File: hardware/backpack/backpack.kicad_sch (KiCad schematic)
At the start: 5 parts, among them J2 Conn_02x06_Top_Bottom, J3 Conn_02x06_Top_Bottom, J7 USB_C, J8 MICROMOD-2222, SW1 BTN_PROGRAM

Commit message: start power
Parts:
- added J8: USB_C, cynthion:USB_C_Receptacle_HRO_TYPE-C-31-M-12, symbol Connector:USB_C_Receptacle_USB2.0
- SW1: value BTN_PROGRAM -> ~; lcsc# (none) -> C692468
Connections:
- new net: J8.A1 (GND), J8.A12 (GND), J8.B1 (GND), J8.B12 (GND)
- new net: J8.A4 (VBUS), J8.A9 (VBUS), J8.B4 (VBUS), J8.B9 (VBUS)
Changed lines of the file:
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@@
+	)
+	(symbol
+		(lib_id "Connector:USB_C_Receptacle_USB2.0")
+		(at 201.93 39.37 0)
+		(mirror y)
+		(unit 1)
+		(exclude_from_sim no)
+		(in_bom yes)
+		(on_board yes)
+		(dnp no)
+		(property "Reference" "J8"
+			(at 201.93 16.51 0)
+			(effects
+				(font
+					(size 1.27 1.27)
+				)
+			)
+		)
+		(property "Value" "USB_C"
+			(at 201.93 19.05 0)
+			(effects
+				(font
+					(size 1.27 1.27)
+				)
+			)
+		)
+		(property "Footprint" "cynthion:USB_C_Receptacle_HRO_TYPE-C-31-M-12"
+			(at 198.12 39.37 0)
+			(effects
+				(font
+					(size 1.27 1.27)
+				)
+				(hide yes)
+			)
+		)
+		(property "Datasheet" ""
+			(at 198.12 39.37 0)
+			(effects
+				(font
+					(size 1.27 1.27)
+				)
+				(hide yes)
+			)
+		)
+		(property "Description" "CONN RCPT USB2.0 TYPE-C 16POS"
+			(at 201.93 39.37 0)
+			(effects
+				(font
+					(size 1.27 1.27)
+				)
+				(hide yes)
+			)
+		)
+		(property "Manufacturer" "DEALON"
+			(at 201.93 39.37 0)
+			(effects
+				(font
+					(size 1.27 1.27)
+				)
+				(hide yes)
+			)
+		)
+		(property "Part Number" "USB-TYPE-C-019"
+			(at 201.93 39.37 0)
+			(effects
+				(font
+					(size 1.27 1.27)
+				)
+				(hide yes)
+			)
+		)
+		(property "Substitution" "Yuandi TYPE-611A-T3"
+			(at 201.93 39.37 0)
+			(effects
+				(font
+					(size 1.27 1.27)
+				)
+				(hide yes)
+			)
+		)
+		(pin "A1"
+		)
+		(pin "A12"
+		)
+		(pin "A4"
+		)
+		(pin "A5"
+		)
+		(pin "A6"
+		)
+		(pin "A7"
+		)
+		(pin "A8"
+		)
+		(pin "A9"
+		)
+		(pin "B1"
+		)
+		(pin "B12"
+		)
+		(pin "B4"
+		)
+		(pin "B5"
+		)
+		(pin "B6"
+		)
+		(pin "B7"
+		)
+		(pin "B8"
+		)
+		(pin "B9"
+		)
+		(pin "S1"
+		)
+		(instances
+			(project "backpack"
+				(path "/df6062c3-a570-4505-924c-c7fe32df3670"
+					(reference "J8")
+					(unit 1)
+				)
+			)
+		)
 	)
 	(symbol
@@
 			)
 		)
-		(property "Value" "BTN_PROGRAM"
+		(property "Value" "~"
 			(at 173.99 46.99 0)
 			(effects
@@
 			(at 173.99 50.8 0)
 			(effects
+				(font
+					(size 1.27 1.27)
+				)
+				(hide yes)
+			)
+		)
+		(property "lcsc#" "C692468"
+			(at 173.99 50.8 0)
+			(effects

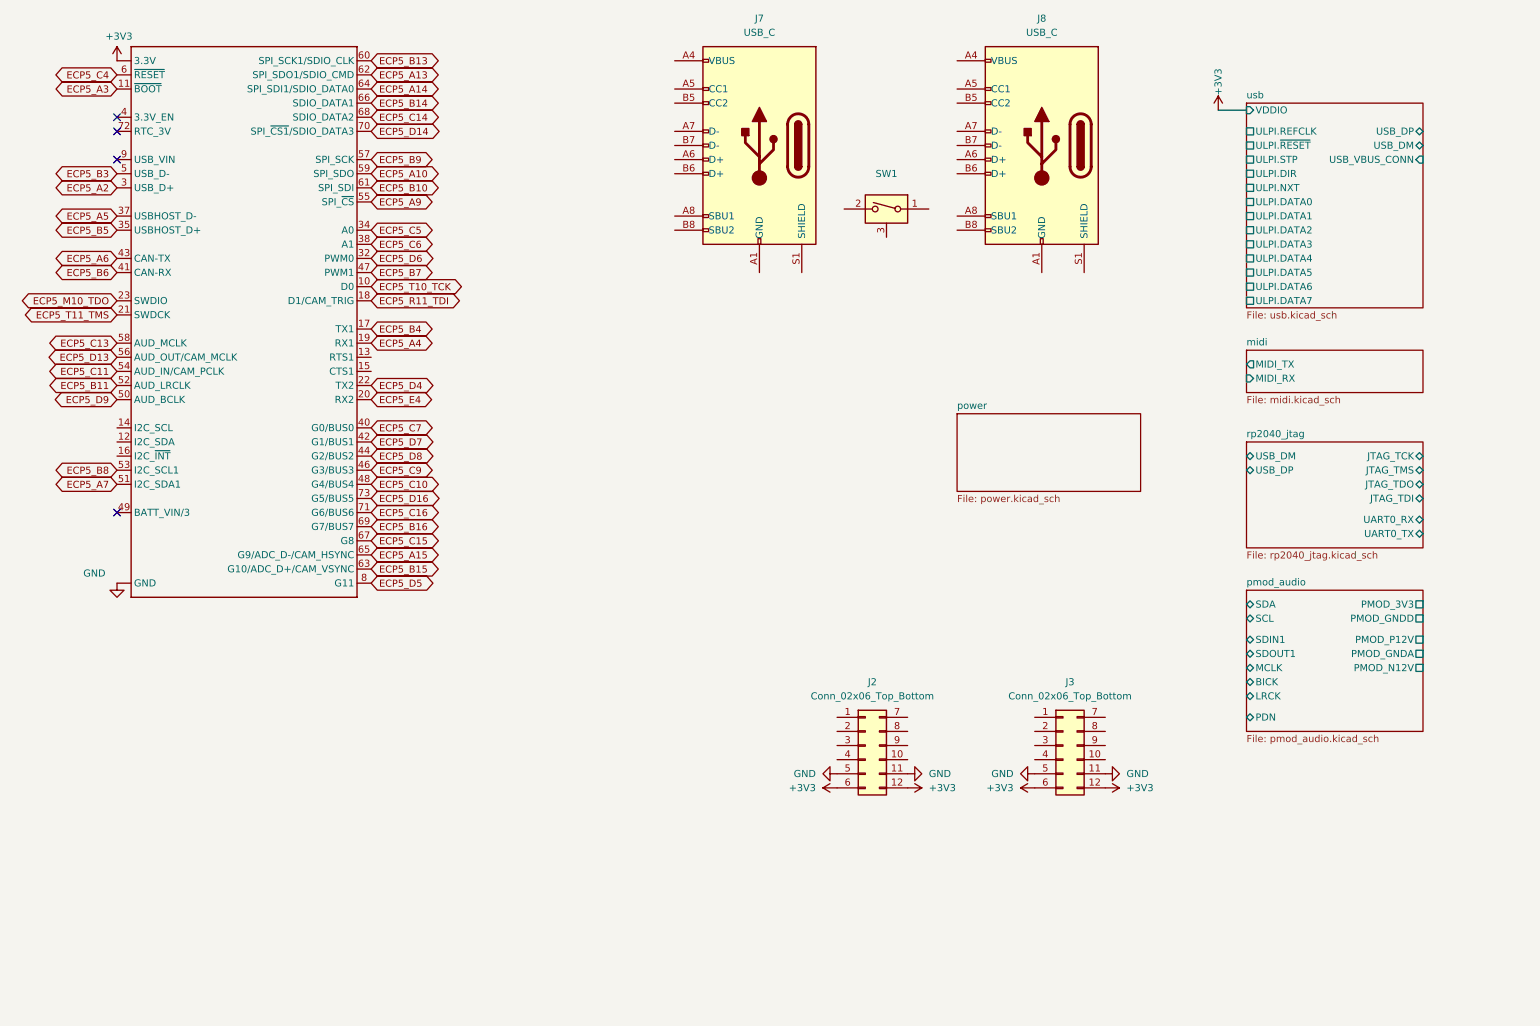
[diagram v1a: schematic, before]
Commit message: parts and capture done sans most needing future pinswaps
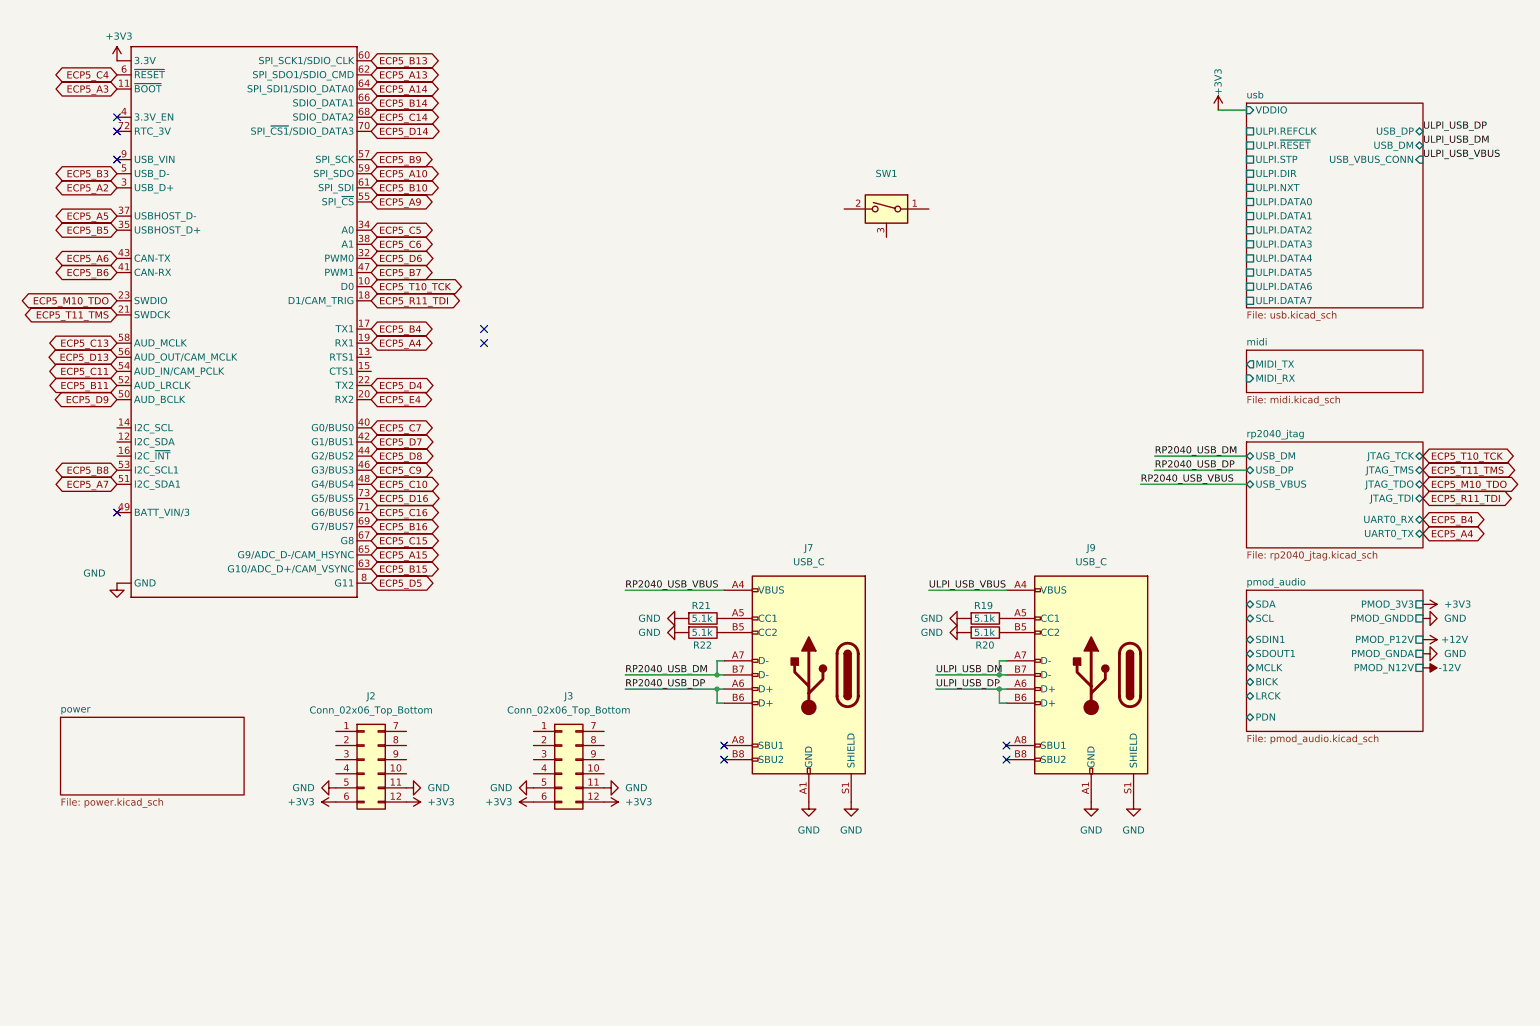
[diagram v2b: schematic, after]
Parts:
- added R19, R20, R21, R22: 5.1k, Resistor_SMD:R_0402_1005Metric, symbol Device:R
- renumbered J8 to J9
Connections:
- net GND: now also J7.A1 (GND), J7.A12 (GND), J7.B1 (GND), J7.B12 (GND), J7.S1 (SHIELD), J9.A1 (GND), J9.A12 (GND), J9.B1 (GND), J9.B12 (GND), J9.S1 (SHIELD), R19.2, R20.2, R21.2, R22.2
- net RP2040_USB_VBUS: now reaches J7.A4 (VBUS), J7.A9 (VBUS), J7.B4 (VBUS), J7.B9 (VBUS)
- net at J7.A5 (CC1): now also R21.1
- net RP2040_USB_DP: now reaches J7.A6 (D+)
- net RP2040_USB_DP: now also J7.B6 (D+)
- net RP2040_USB_DM: now reaches J7.A7 (D-)
- net RP2040_USB_DM: now also J7.B7 (D-)
- net at J7.B5 (CC2): now also R22.1
- net ULPI_USB_VBUS: now reaches J9.A4 (VBUS), J9.A9 (VBUS), J9.B4 (VBUS), J9.B9 (VBUS)
- net at J9.A5 (CC1): now also R19.1
- net ULPI_USB_DP: now reaches J9.A6 (D+)
- net ULPI_USB_DP: now also J9.B6 (D+)
- net ULPI_USB_DM: now reaches J9.A7 (D-)
- net ULPI_USB_DM: now also J9.B7 (D-)
- net at J9.B5 (CC2): now also R20.1
- no-connect marks 4 -> 10
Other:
- sheet rp2040_jtag ports: added USB_VBUS; removed none
- moved on the sheet: J2, J3, J7, J9

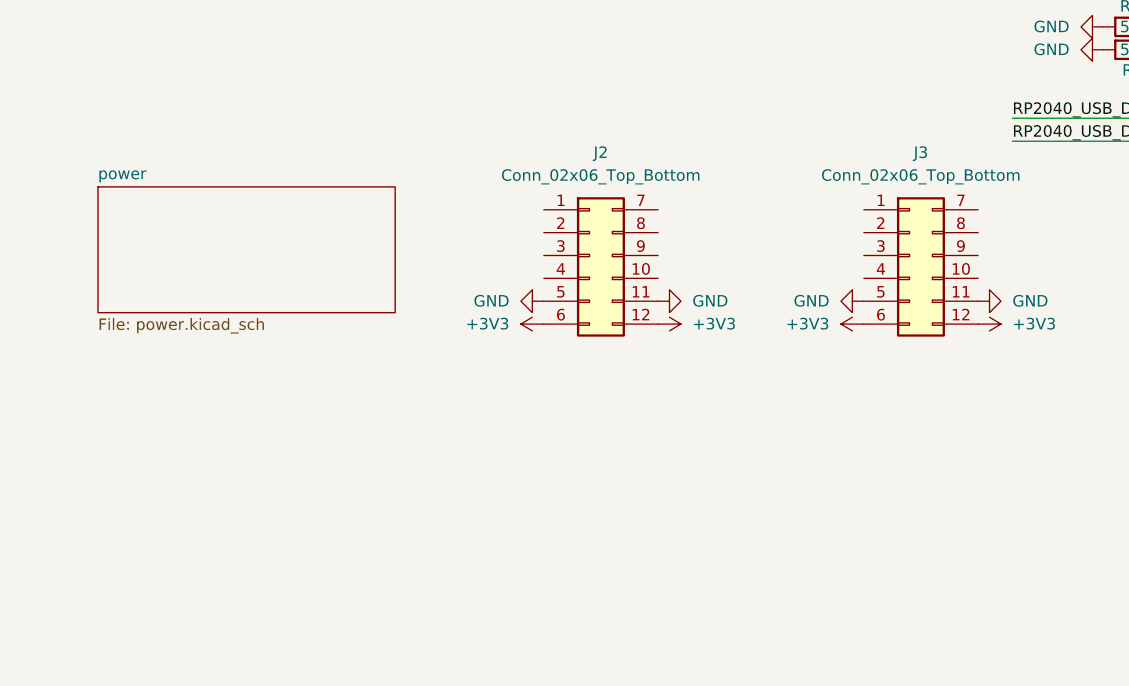
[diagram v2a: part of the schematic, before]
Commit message: aux vin over usb
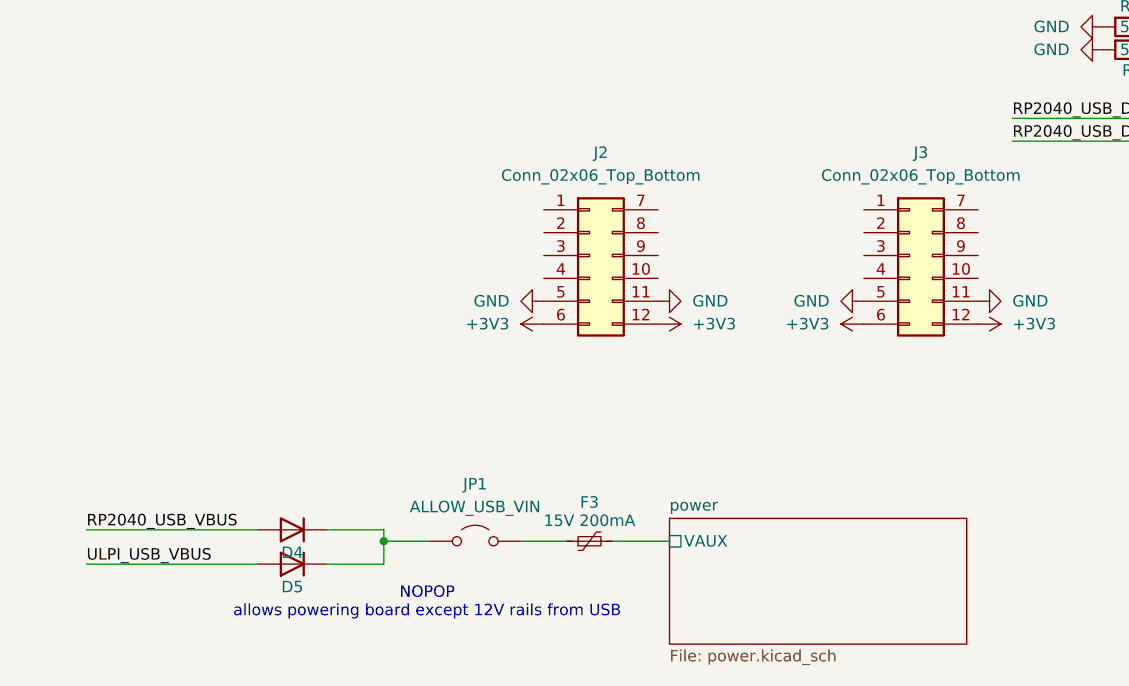
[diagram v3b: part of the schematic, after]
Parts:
- added D4, D5: 1N4007FL, Diode_SMD:D_SOD-123F, symbol Diode:US1G
- added F3: 15V 200mA, Fuse:Fuse_0805_2012Metric, symbol Device:Polyfuse_Small
- added JP1: ALLOW_USB_VIN, symbol Jumper:Jumper_2_Open
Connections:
- net RP2040_USB_VBUS: now also D4.2 (A)
- net ULPI_USB_VBUS: now also D5.2 (A)
- new net: D4.1 (K), D5.1 (K), JP1.1 (A)
- new net: F3.1, JP1.2 (B)
- new net power/VAUX: F3.2
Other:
- sheet power ports: added VAUX; removed none
- note added: "NOPOP allows powering board except 12V rails from USB"

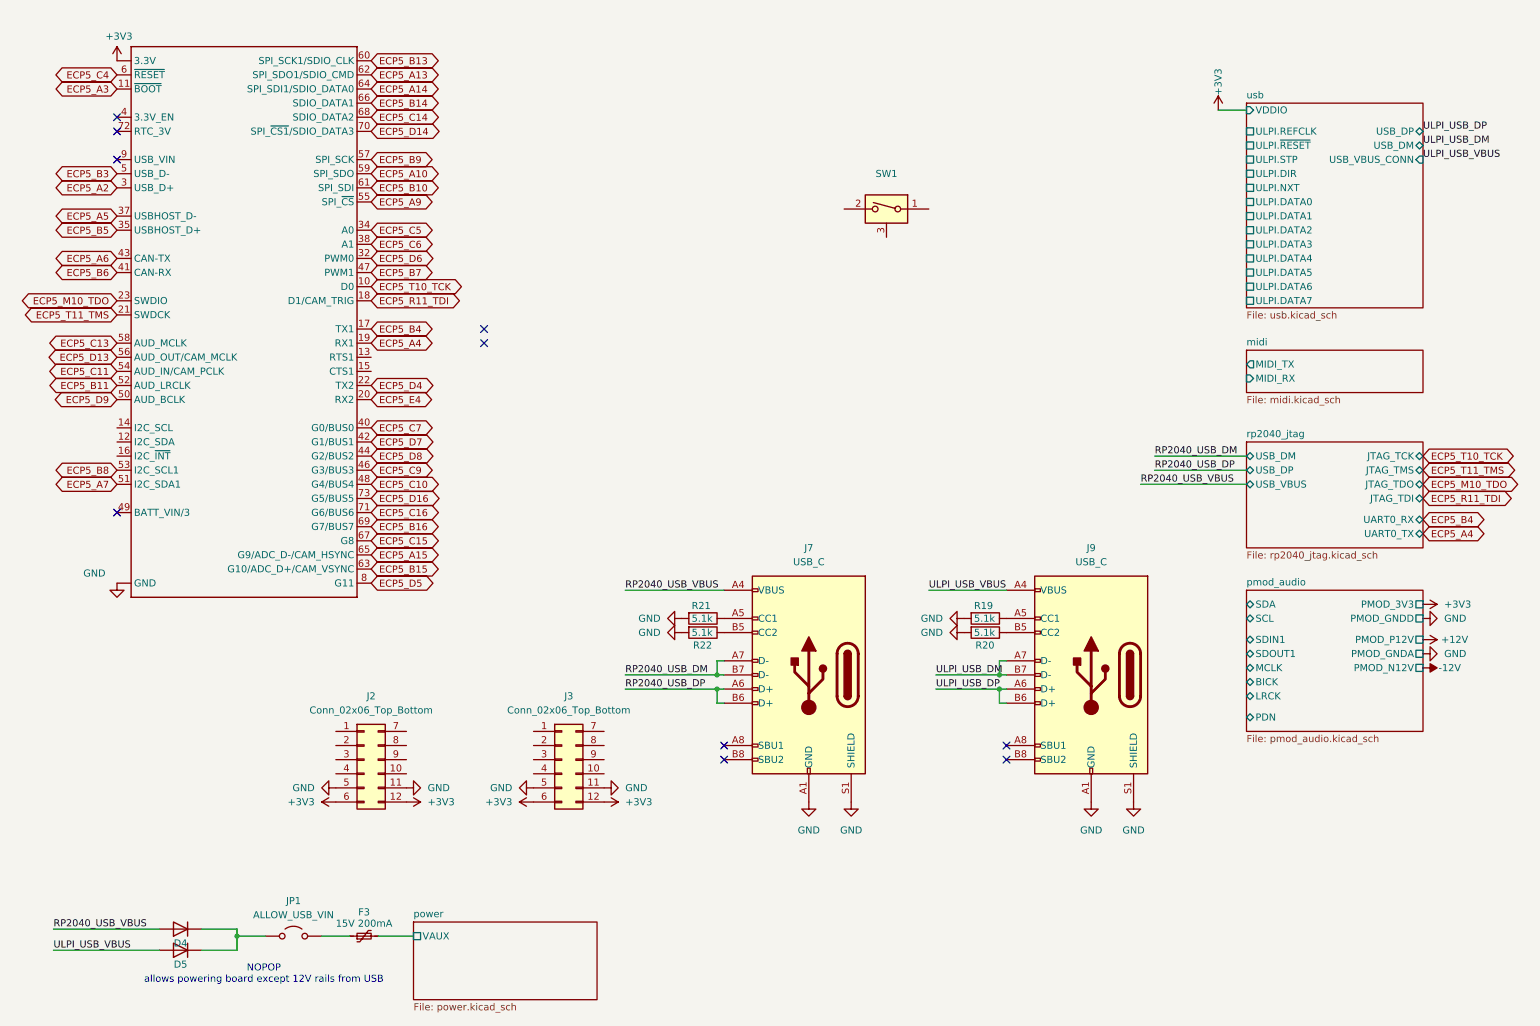
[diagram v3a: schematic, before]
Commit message: connections + placement done
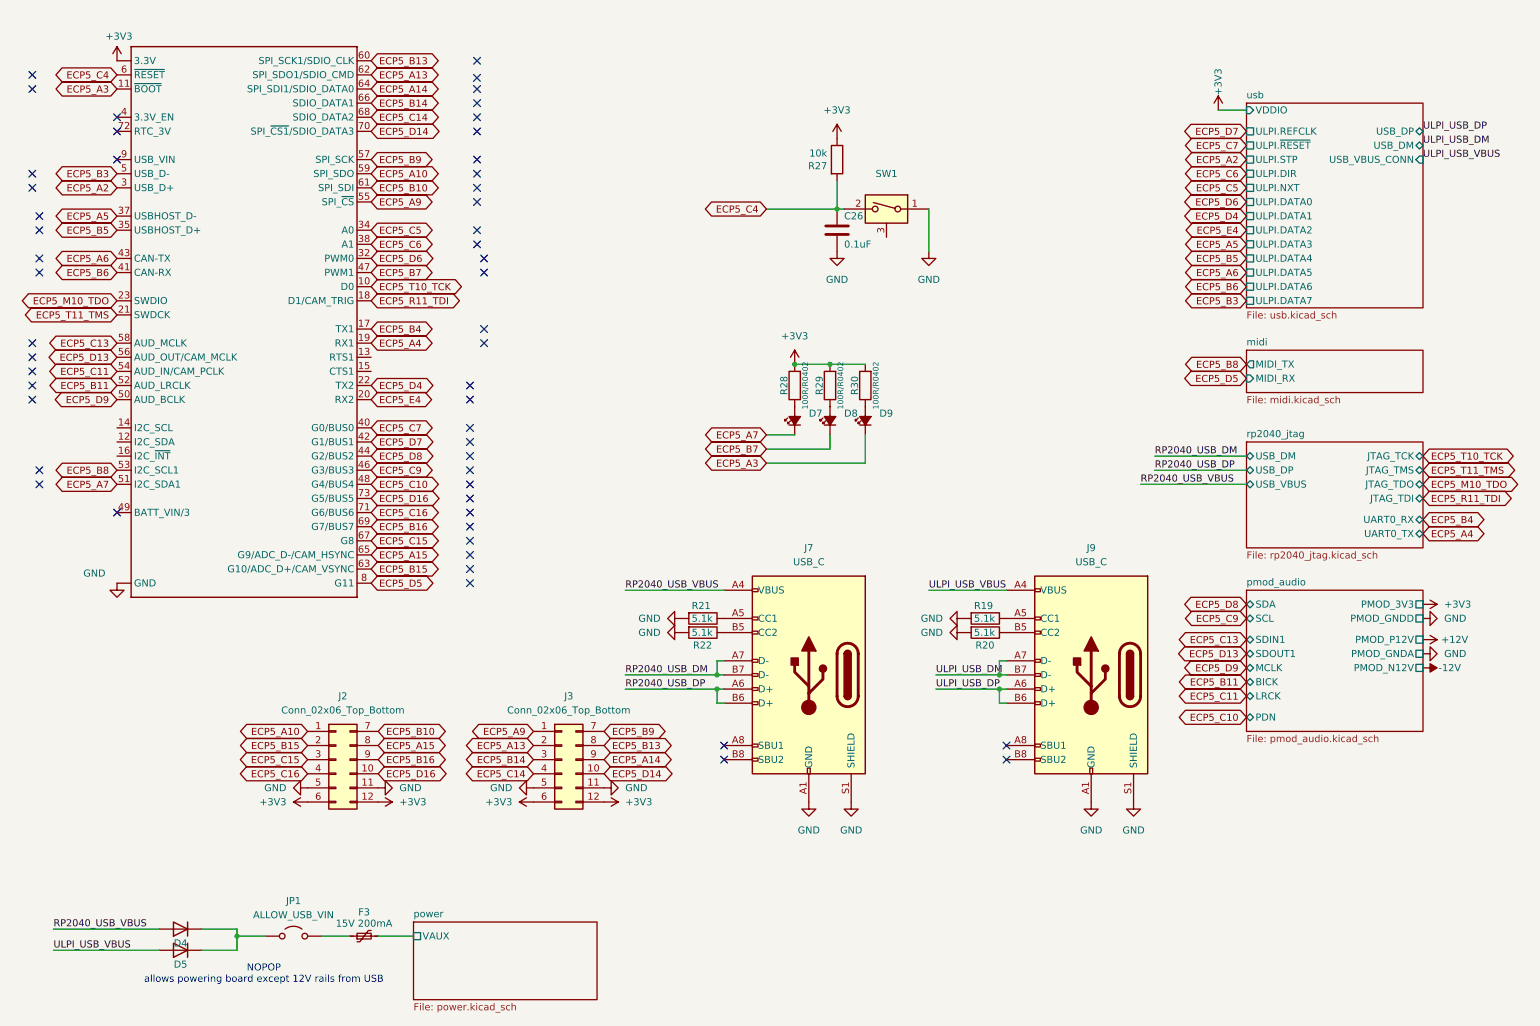
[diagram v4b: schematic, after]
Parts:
- added C26: 0.1uF, Capacitor_SMD:C_0402_1005Metric, symbol Device:C
- added D7, D8, D9: LED 0402 RED, LED_SMD:LED_0402_1005Metric, symbol Device:LED_Small_Filled
- added R27: 10k, Resistor_SMD:R_0402_1005Metric, symbol Device:R
- added R28, R29, R30: 100R/R0402, Resistor_SMD:R_0402_1005Metric, symbol OLIMEX_RCL:R
- JP1: footprint (none) -> Jumper:SolderJumper-2_P1.3mm_Open_RoundedPad1.0x1.5mm
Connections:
- net +3V3: now also R27.1, R28.2, R29.2, R30.2
- net ECP5_A10: now also J2.1 (Pin_1)
- net ECP5_A13: now also J3.2 (Pin_2)
- net ECP5_A14: now also J3.9 (Pin_9)
- net ECP5_A15: now also J2.8 (Pin_8)
- net ECP5_A3: now also D9.1 (K)
- net ECP5_A7: now also D7.1 (K)
- net ECP5_A9: now also J3.1 (Pin_1)
- net ECP5_B10: now also J2.7 (Pin_7)
- net ECP5_B13: now also J3.8 (Pin_8)
- net ECP5_B14: now also J3.3 (Pin_3)
- net ECP5_B15: now also J2.2 (Pin_2)
- net ECP5_B16: now also J2.9 (Pin_9)
- net ECP5_B7: now also D8.1 (K)
- net ECP5_B9: now also J3.7 (Pin_7)
- net ECP5_C14: now also J3.4 (Pin_4)
- net ECP5_C15: now also J2.3 (Pin_3)
- net ECP5_C16: now also J2.4 (Pin_4)
- net ECP5_C4: now also SW1.2, C26.1, R27.2
- net ECP5_D14: now also J3.10 (Pin_10)
- net ECP5_D16: now also J2.10 (Pin_10)
- net GND: now also SW1.1, C26.2
- new net: D9.2 (A), R30.1
- new net: D8.2 (A), R29.1
- new net: D7.2 (A), R28.1
- no-connect marks 10 -> 53
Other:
- moved on the sheet: J2
